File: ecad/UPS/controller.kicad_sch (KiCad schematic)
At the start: 32 parts, among them J2 Conn_01x05_Socket, SW1 SW_Push, SW2 SW_Push, U1 STM32L152RCT6, U2 AP2112K-3.3TRG1

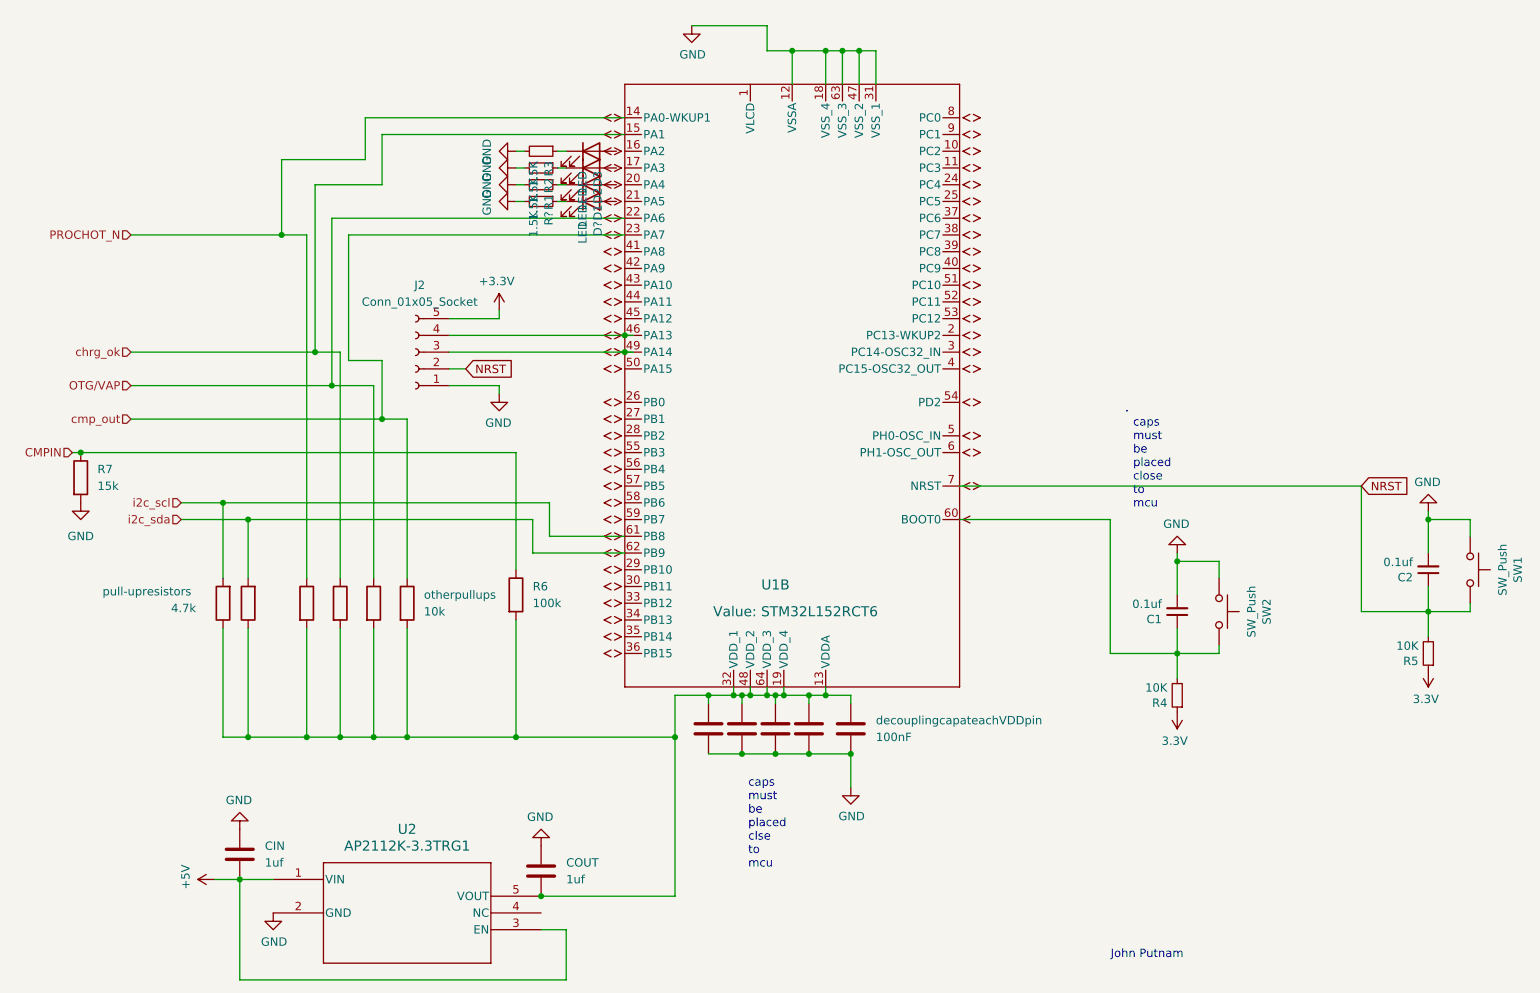
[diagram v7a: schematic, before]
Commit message: added components to bom
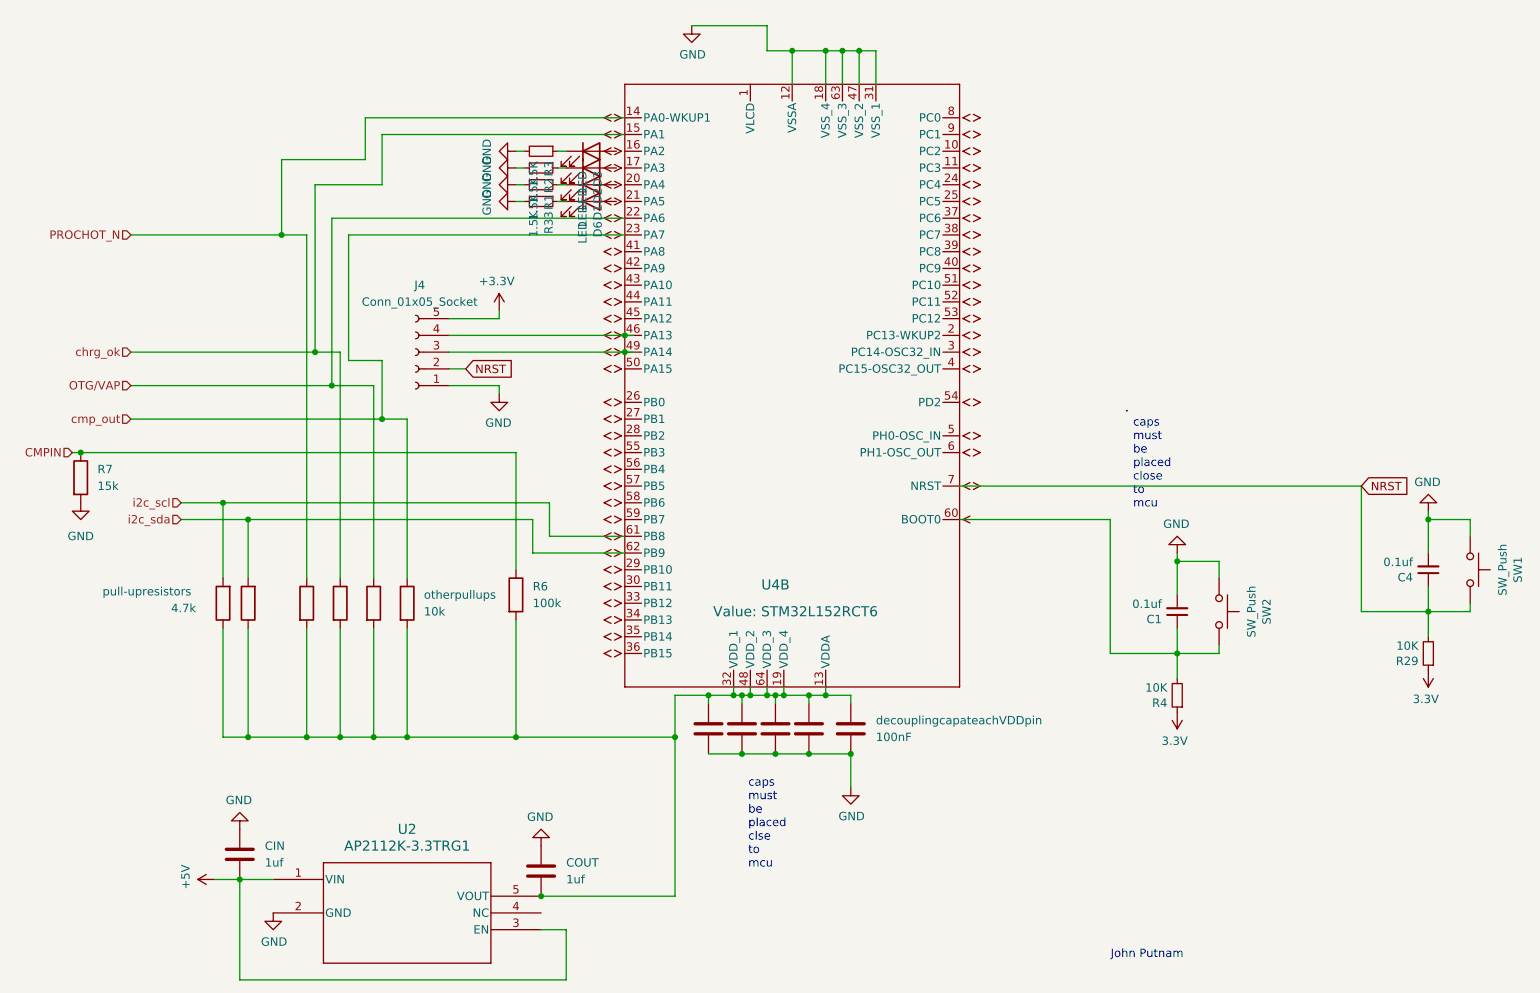
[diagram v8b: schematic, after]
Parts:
- gave numbers to parts that had none: 2
- renumbered C2 to C4, J2 to J4, R5 to R29, U1 to U4
